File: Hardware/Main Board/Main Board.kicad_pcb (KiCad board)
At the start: 2 copper layers, 55 parts, among them Q1 MMBT3904-TP, Q2 MMBT3904-TP, Q3 A04484, U1 MT3608, U3 ATtiny1614

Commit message: Added base code for take 3 of beat detection. We got thisgit add .!
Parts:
- added SW1: Momentary, Button_Switch_SMD:SW_SPST_PTS645, F.Cu at (109.5, 78.7)
- added TP4: GND, TestPoint:TestPoint_Pad_D2.5mm, F.Cu at (116.6, 102.4)
- added U2: NCP718A, Main Board:wdfn, F.Cu at (118.1, 79.5)
- L1: footprint Inductor_SMD:L_Abracon_ASPI-3012S -> Inductor_SMD:L_Bourns_SRN6045TA
- Q3: footprint Package_TO_SOT_SMD:TDSON-8-1 -> Package_SO:SOIC-8_3.9x4.9mm_P1.27mm
- moved R15 86.1 mm to (94.2, 79.5)
- moved R16 85.3 mm to (94.2, 76.5)
- moved R12 84.7 mm to (116.6, 66.3)
- moved C6 81.1 mm to (151.9, 78.2)
- moved R14 78.2 mm to (110.5, 78.7)
- moved R13 77.8 mm to (115.8, 69.2)
- moved C4 77.8 mm to (91.2, 94.2)
- moved TP13 77.1 mm to (89.9, 77.2)
- moved R20 76.9 mm to (119.9, 75.7)
- moved C9 74.3 mm to (107.4, 83.8)
- moved U1 73.5 mm to (98.8, 82.8), turned to 90 degrees
- moved TP7 73.2 mm to (89.2, 82.8)
- moved TH1 71.8 mm to (94.2, 84.3)
- moved TP9 69.8 mm to (89.7, 88.6)
- moved Q3 67.8 mm to (125.7, 78.7)
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
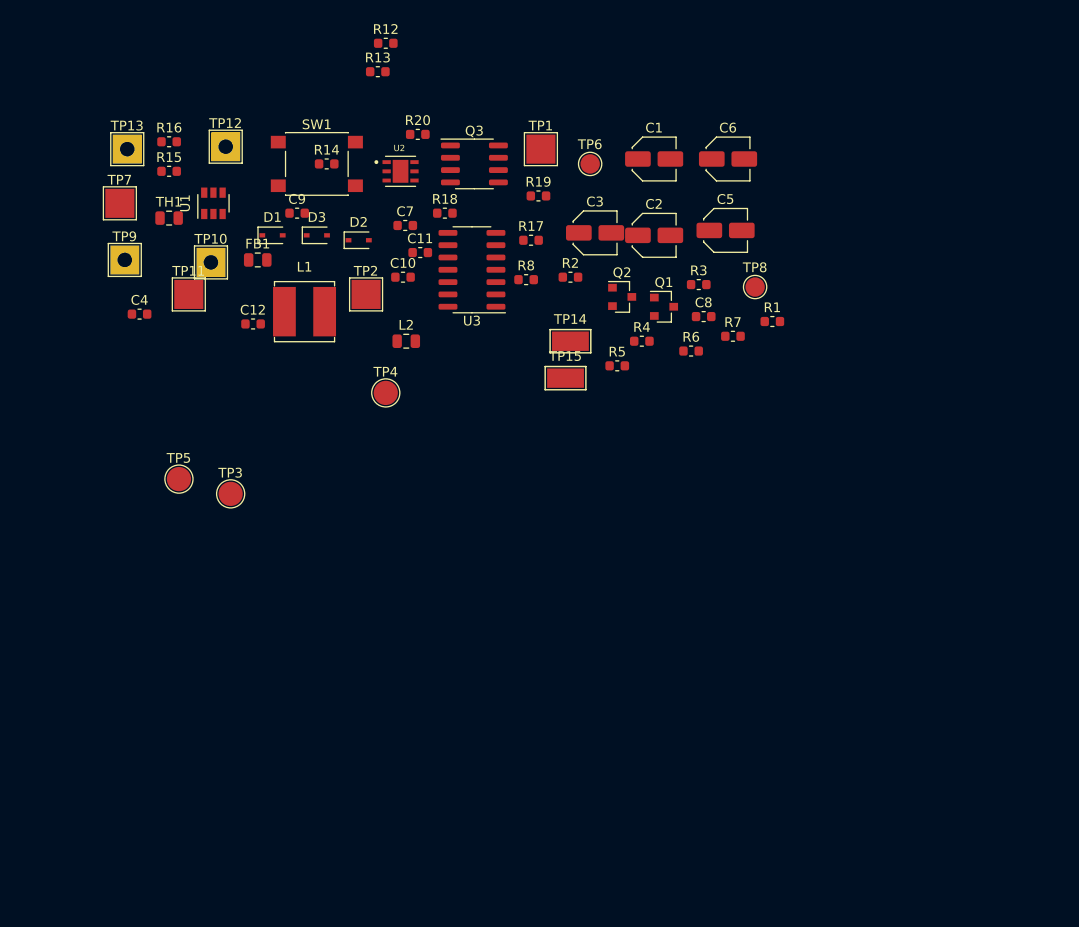
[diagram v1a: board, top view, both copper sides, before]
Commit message: placed PCB
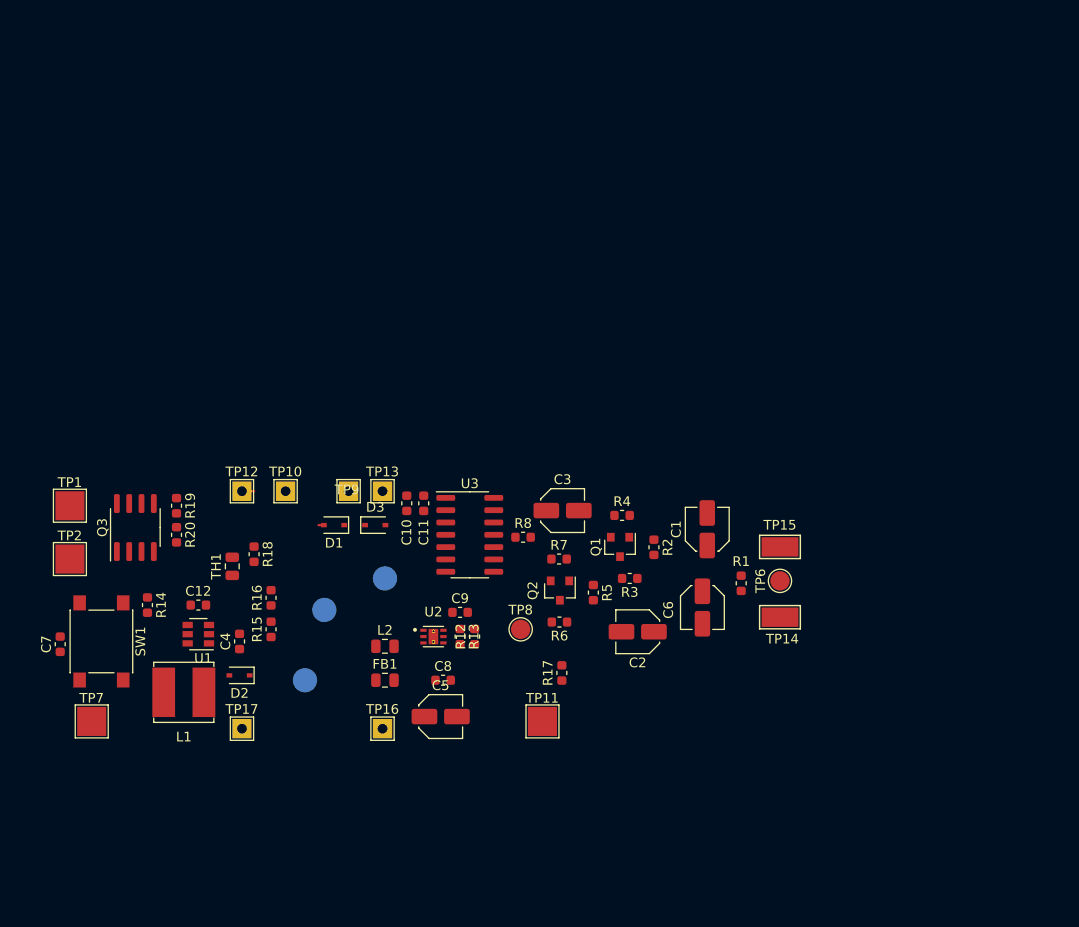
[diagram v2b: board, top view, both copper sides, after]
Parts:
- added TP16: Support, TestPoint:TestPoint_THTPad_2.0x2.0mm_Drill1.0mm, F.Cu at (116.2, 137.0)
- added TP17: Support, TestPoint:TestPoint_THTPad_2.0x2.0mm_Drill1.0mm, F.Cu at (101.8, 137.0)
- TP10, TP12, TP13, TP9: footprint TestPoint:TestPoint_THTPad_3.0x3.0mm_Drill1.5mm -> TestPoint:TestPoint_THTPad_2.0x2.0mm_Drill1.0mm
- TP3, TP4, TP5: moved to B.Cu
- U2: footprint Main Board:wdfn -> Footprints:SON65P200X200X80-7N
- moved R12 61.9 mm to (125.8, 127.5), turned to 90 degrees
- moved TP1 60.9 mm to (84.0, 114.0)
- moved R13 58.9 mm to (124.2, 127.5), turned to 270 degrees
- moved C5 58.1 mm to (122.2, 135.8)
- moved TP11 57.2 mm to (132.8, 136.2)
- moved C7 56.0 mm to (83.0, 128.3), turned to 90 degrees
- moved SW1 54.0 mm to (87.2, 128.0), turned to 270 degrees
- moved TP7 53.5 mm to (86.2, 136.2)
- moved Q3 51.3 mm to (90.8, 116.2), turned to 90 degrees
- moved R19 49.1 mm to (95.0, 114.0), turned to 270 degrees
- moved R14 49.1 mm to (92.0, 124.2), turned to 270 degrees
- moved R15 48.4 mm to (104.8, 126.8), turned to 90 degrees
- moved R20 48.2 mm to (95.0, 117.0), turned to 270 degrees
- moved R16 48.2 mm to (104.8, 123.5), turned to 90 degrees
- moved U2 48.1 mm to (121.5, 127.5)
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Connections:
- R16 pad 2: GNDA -> GNDPWR
- U1 pad 1: (no net) -> Net-(D2-Pad2)
- U1 pad 2: (no net) -> GNDPWR
- U1 pad 3: (no net) -> Net-(R15-Pad2)
- U1 pad 4: (no net) -> /MAIN_POWER
- U1 pad 5: (no net) -> +3V3
- U3 pad 10: /PRMG -> /PRGM
- U3 pad 13: Net-(U3-Pad13) -> (no net)
- U3 pad 2: Net-(U3-Pad2) -> (no net)
- U3 pad 3: Net-(U3-Pad3) -> (no net)
- U3 pad 4: Net-(U3-Pad4) -> (no net)
- U3 pad 5: Net-(U3-Pad5) -> (no net)
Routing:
- net +3V3: track 0.00 -> 1.80 mm

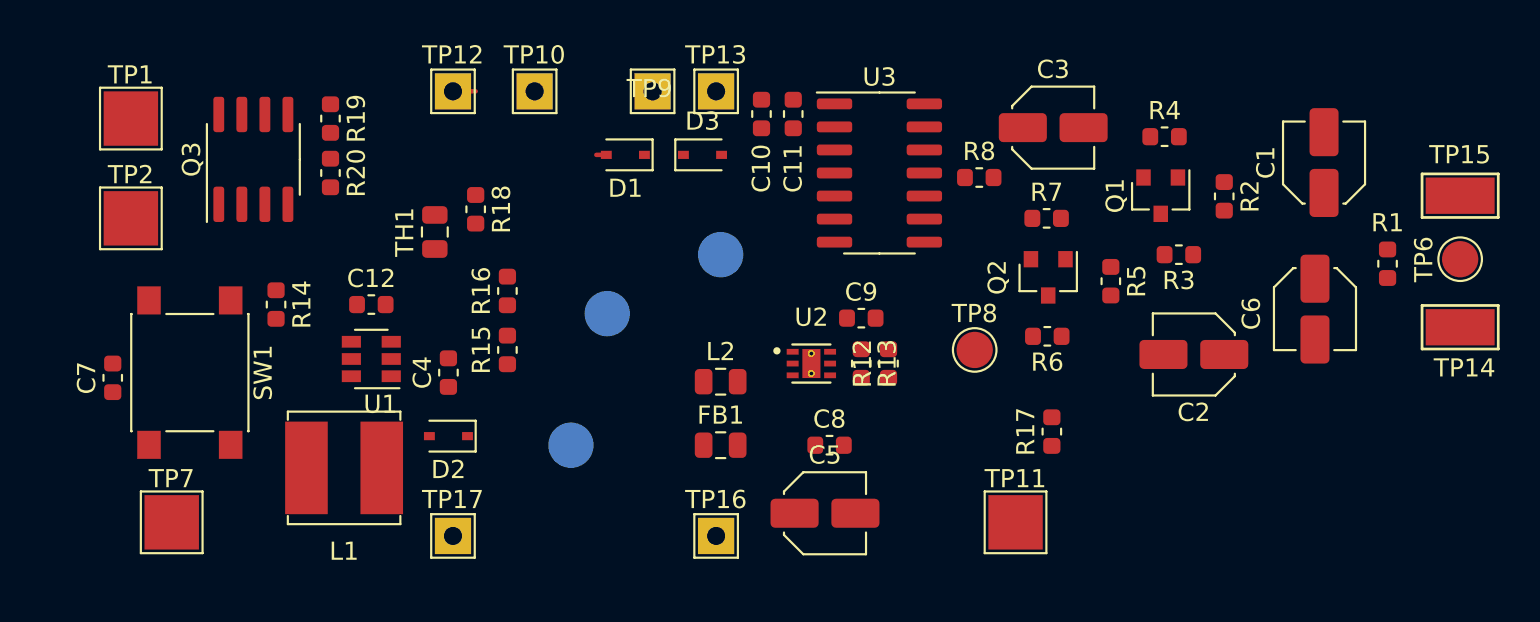
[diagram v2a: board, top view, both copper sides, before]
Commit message: coper fills on PCB
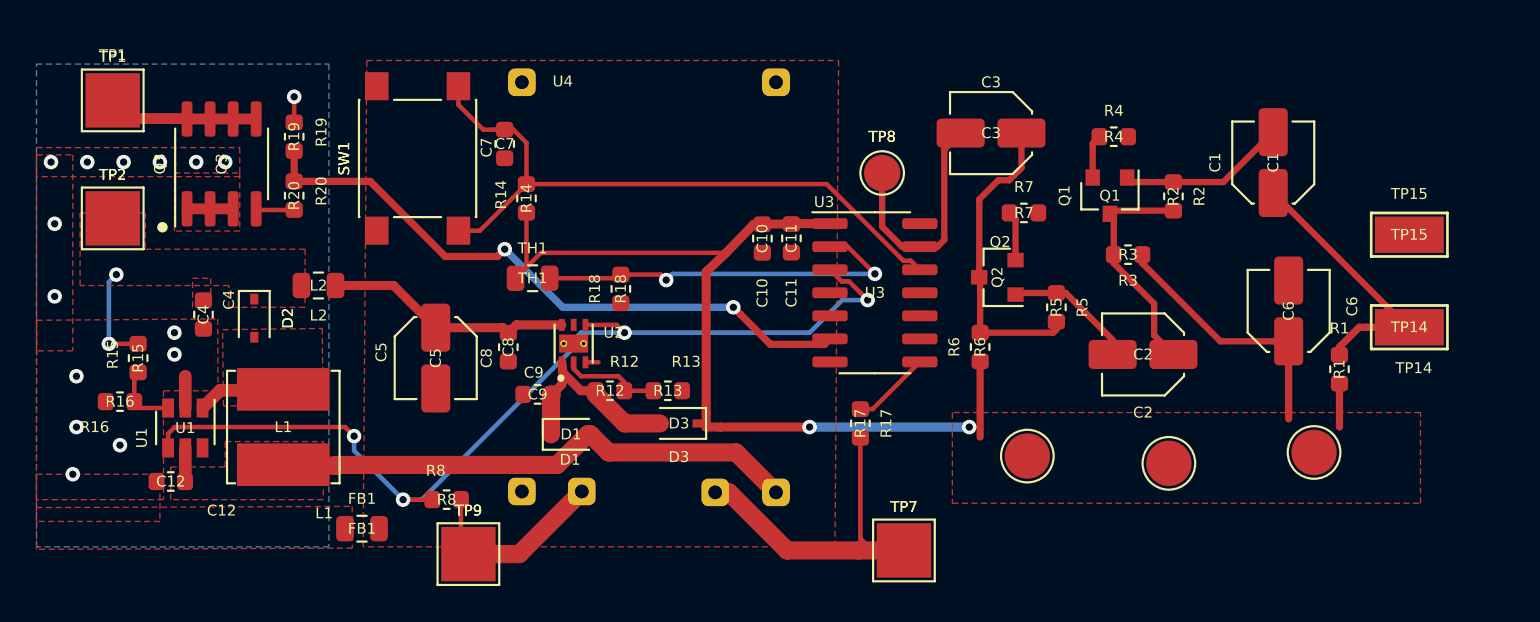
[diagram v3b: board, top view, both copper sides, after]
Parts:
- removed TP10: B-, TestPoint:TestPoint_THTPad_2.0x2.0mm_Drill1.0mm
- removed TP11: Battery-, TestPoint:TestPoint_Pad_3.0x3.0mm
- removed TP12: P+, TestPoint:TestPoint_THTPad_2.0x2.0mm_Drill1.0mm
- removed TP13: P-, TestPoint:TestPoint_THTPad_2.0x2.0mm_Drill1.0mm
- removed TP16, TP17: Support, TestPoint:TestPoint_THTPad_2.0x2.0mm_Drill1.0mm
- removed TP6: 3V, TestPoint:TestPoint_Pad_D2.0mm
- added U4: TP4056, Main Board1:charger, F.Cu at (120.0, 138.2)
- Q3: value A04484 -> AO4484; footprint Package_SO:SOIC-8_3.9x4.9mm_P1.27mm -> Main Board1:SOIC-8_3.9x4.9mm_P1.27mm
- TP3, TP4, TP5: moved to F.Cu
- TP9: value B+ -> Battery-; footprint TestPoint:TestPoint_THTPad_2.0x2.0mm_Drill1.0mm -> TestPoint:TestPoint_Pad_3.0x3.0mm
- moved TP7 40.4 mm to (126.6, 137.8)
- moved TP4 39.7 mm to (149.2, 132.4)
- moved R8 34.3 mm to (101.4, 135.0), turned to 180 degrees
- moved TP3 33.0 mm to (141.2, 133.0)
- moved TP9 27.4 mm to (102.6, 138.0)
- moved C7 25.2 mm to (104.6, 115.4), turned to 270 degrees
- moved C5 23.1 mm to (100.8, 127.2), turned to 270 degrees
- moved L2 22.8 mm to (94.3, 123.2), turned to 180 degrees
- moved R16 22.2 mm to (83.4, 129.6), turned to 180 degrees
- moved R15 20.4 mm to (84.4, 127.2), turned to 270 degrees
- moved FB1 20.3 mm to (96.7, 136.6)
- moved TP5 20.2 mm to (133.4, 132.6)
- moved C8 18.5 mm to (104.8, 126.6), turned to 270 degrees
- moved C9 18.3 mm to (106.4, 129.2), turned to 180 degrees
- moved SW1 17.2 mm to (99.8, 116.2), turned to 90 degrees
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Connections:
- net Net-(Q3-Pad4) renamed /G
- net Net-(Q3-Pad5) renamed /D
- R8 pad 1: GNDA -> GNDREF
- R8 pad 2: /MAIN_POWER -> /EN
- TP9 pad 1: +BATT -> GNDREF
- U1 pad 4: /MAIN_POWER -> /EN
- U2 pad 4: /MAIN_POWER -> /EN
- U3 pad 11: /PACK_SENSE -> (no net)
- U3 pad 12: /MAIN_POWER -> /MODE
- U3 pad 13: (no net) -> /MIC_IN
- U3 pad 2: (no net) -> /TEMP_SENSE
- U3 pad 3: (no net) -> /EN
- U3 pad 7: /MODE -> (no net)
- U3 pad 8: /TEMP_SENSE -> /PACK_SENSE
- U3 pad 9: /MIC_IN -> (no net)
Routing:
- net +5V: track 0.00 -> 68.7 mm, vias 0 -> 2
- net /EN: track 0.00 -> 53.3 mm, vias 0 -> 4
- net /MODE: track 0.00 -> 36.4 mm
- net /LED: track 0.00 -> 35.4 mm, vias 0 -> 2
- net +3V3: track 1.80 -> 31.7 mm
- net /TEMP_SENSE: track 0.00 -> 21.5 mm, vias 0 -> 2
- net +BATT: track 0.00 -> 20.0 mm
- net Net-(C3-Pad1): track 0.00 -> 17.3 mm
- net Net-(C1-Pad1): track 0.00 -> 16.0 mm
- net Net-(C5-Pad1): track 0.00 -> 14.1 mm
- net /MIC_IN: track 0.00 -> 13.3 mm
- net Net-(C2-Pad1): track 0.00 -> 12.8 mm
- net Net-(C9-Pad1): track 0.00 -> 11.1 mm
- net GNDREF: track 0.00 -> 10.8 mm
- net Net-(C1-Pad2): track 0.00 -> 9.29 mm
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- added copper zone on F.Cu, net +10V
- added copper zone on F.Cu, net +3V3
- added copper zone on F.Cu, net +5V
- added copper zone on F.Cu, net GNDA
- added copper zone on B.Cu, net GNDPWR
- added copper zone on F.Cu, net GNDPWR
- added copper zone on F.Cu, net Net-(D2-Pad2)

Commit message: almost done pcb
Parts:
- TP3, TP4, TP5: moved to B.Cu
- moved TP4 37.2 mm to (114.6, 118.9)
- moved TP3 17.2 mm to (125.3, 126.3)
- moved C10 1.77 mm to (118.9, 118.8), turned to 90 degrees
- moved C11 1.73 mm to (120.5, 118.9), turned to 90 degrees
- moved TP5 0.44 mm to (133.0, 132.4)
- moved TP7 0.23 mm to (126.8, 137.9)
- moved TP9 0.13 mm to (102.6, 137.9)
- moved D3 0.10 mm to (114.3, 130.8)
- turned FB1 to 180 degrees
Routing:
- net GNDPWR: track 5.70 -> 20.2 mm, vias 15 -> 27
- net /PRGM: track 0.00 -> 5.49 mm, vias 0 -> 1
- net +5V: track 68.7 -> 71.6 mm, vias 2 -> 3
- net /MODE: track 36.4 -> 38.0 mm
- net Net-(C9-Pad1): track 11.1 -> 11.9 mm
- net GNDA: vias 0 -> 47
- added copper zone on B.Cu, net GNDA

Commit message: PCB completed and ready for reviewgit add .git add .
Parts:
- added G***: LOGO, 1, F.Cu at (165.8, 105.3)
- added G***: LOGO, 123332343423, B.Cu at (139.7, 93.5)
- added G***: LOGO, 3333, B.Cu at (180.5, 101.7)
- added G***: LOGO, ddr, F.Cu at (0.00, 0.00)
- added REF**: MountingHole_2.2mm_M2, MountingHole:MountingHole_2.2mm_M2, F.Cu at (181.7, 87.7)
- moved TP4 45.3 mm to (148.2, 88.7)
- moved TP5 40.4 mm to (162.1, 104.4)
- moved R8 39.6 mm to (130.1, 107.7)
- moved TP9 39.6 mm to (131.2, 110.5)
- moved TP7 39.5 mm to (155.3, 110.5)
- moved C11 39.1 mm to (149.1, 92.3)
- moved C12 39.1 mm to (114.8, 107.4)
- moved C2 39.1 mm to (168.4, 100.4)
- moved C7 39.1 mm to (133.2, 88.8)
- moved D2 39.1 mm to (119.4, 98.4)
- moved Q1 39.1 mm to (166.5, 91.6)
- moved Q2 39.1 mm to (160.3, 96.1)
- moved Q3 39.1 mm to (117.6, 89.9)
- moved R1 39.1 mm to (179.2, 101.2)
- moved R12 39.1 mm to (139.0, 102.4)
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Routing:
- net +10V: track 5.86 -> 4.14 mm, vias 2 -> 0
- net GNDREF: track 10.8 -> 10.3 mm
- net GNDPWR: vias 27 -> 29
- net GNDA: vias 47 -> 52
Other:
- board outline added: 78.7 x 29.1 mm
- board text added: "10V 0.7A MAX 3V 1.5A MAX"
- board text added: "10V+"
- board text added: "3V+"
- board text added: "B+"
- board text added: "B-"
- board text added: "DAVID "DDR" ROBERTS"
- board text added: "G"
- board text added: "GND"
- board text added: "MICHAEL "CORNFLAKES" MADI"
- board text added: "PGM"
- board text added: "V"

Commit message: PCB fixeruppers
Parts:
- C1, C2, C3: footprint Capacitor_SMD:C_Elec_4x5.4 -> Main Board:CP_Elec_4x3
- C5, C6: footprint Capacitor_SMD:C_Elec_4x5.4 -> Main Board:100
- moved R1 2.56 mm to (181.5, 102.4)
- moved C6 0.68 mm to (175.9, 98.4)
- moved C5 0.62 mm to (128.8, 100.6)
- moved C1 0.56 mm to (175.0, 89.7), turned to 180 degrees
- moved L2 0.34 mm to (122.6, 96.5)
- moved C2 0.33 mm to (168.2, 100.1)
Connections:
- U1 pad 6: (no net) -> Net-(U1-Pad6)
- U3 pad 11: (no net) -> Net-(U3-Pad11)
- U3 pad 4: (no net) -> Net-(U3-Pad4)
- U3 pad 5: (no net) -> Net-(U3-Pad5)
- U3 pad 7: (no net) -> Net-(U3-Pad7)
- U3 pad 9: (no net) -> Net-(U3-Pad9)
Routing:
- net +5V: track 71.6 -> 67.1 mm
- net Net-(C1-Pad2): track 9.29 -> 6.42 mm
- net Net-(C2-Pad2): track 7.26 -> 6.60 mm
- net Net-(C1-Pad1): track 16.0 -> 16.6 mm
- net GNDA: vias 52 -> 54
- net (no net): vias 0 -> 1

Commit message: added marketing folder. we should maybe make a G drive soon if we start filling up.
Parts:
- L1: footprint Inductor_SMD:L_Bourns_SRN6045TA -> Main Board:BW10uHInductor
- moved FB1 0.28 mm to (125.1, 109.9)
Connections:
- U3 pad 12: /MODE -> Net-(U3-Pad12)
- U3 pad 2: /TEMP_SENSE -> Net-(U3-Pad2)
- U3 pad 3: /EN -> /MODE
- U3 pad 4: Net-(U3-Pad4) -> /TEMP_SENSE
- U3 pad 5: Net-(U3-Pad5) -> /EN
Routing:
- net /MODE: track 38.0 -> 27.1 mm, vias 0 -> 2
- net /TEMP_SENSE: track 21.5 -> 16.1 mm
- net /EN: track 53.9 -> 48.7 mm
- net GNDA: track 0.72 -> 3.05 mm, vias 54 -> 49
- net Net-(D2-Pad2): track 5.58 -> 4.20 mm
- net /MIC_IN: track 13.3 -> 14.3 mm
- net GNDPWR: track 20.2 -> 20.4 mm, vias 29 -> 33
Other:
- outline, holes or cut-outs redrawn
